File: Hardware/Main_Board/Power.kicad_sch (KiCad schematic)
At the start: 5 parts, among them U2 LM2596DSADJG

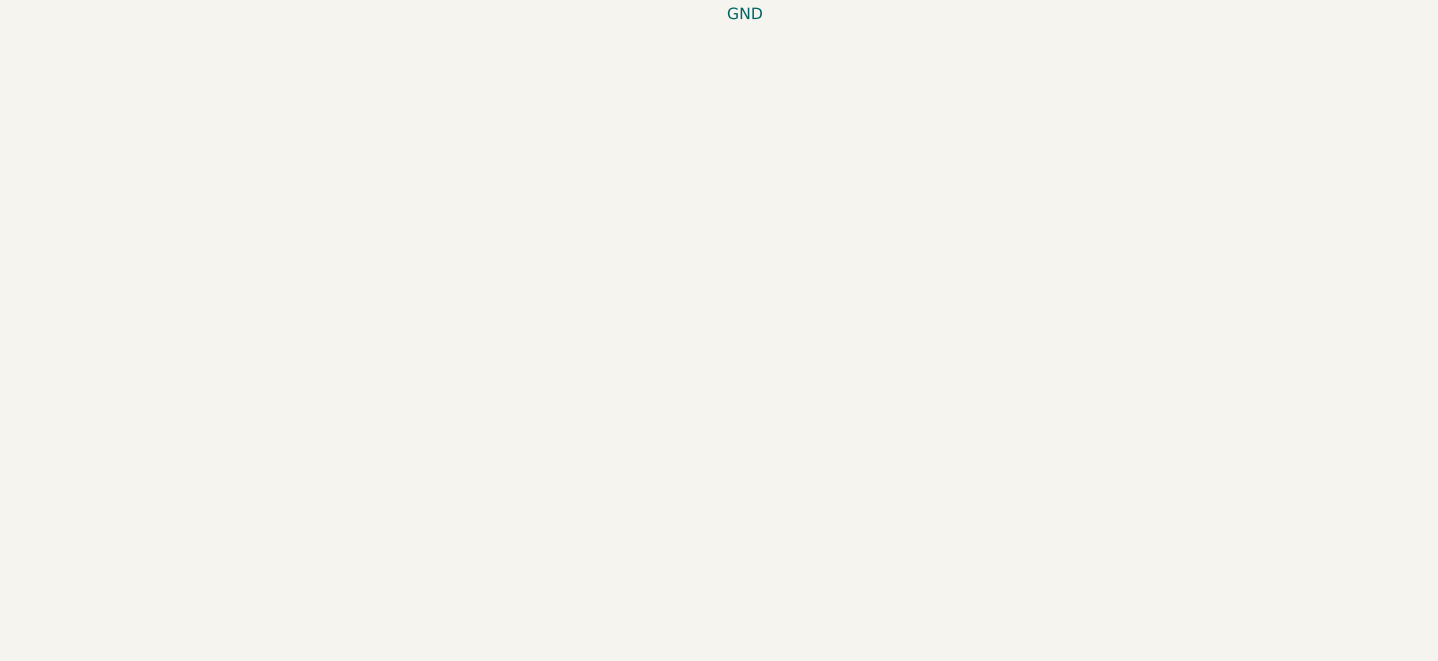
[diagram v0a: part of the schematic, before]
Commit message: Added the LDO on the Power schematic
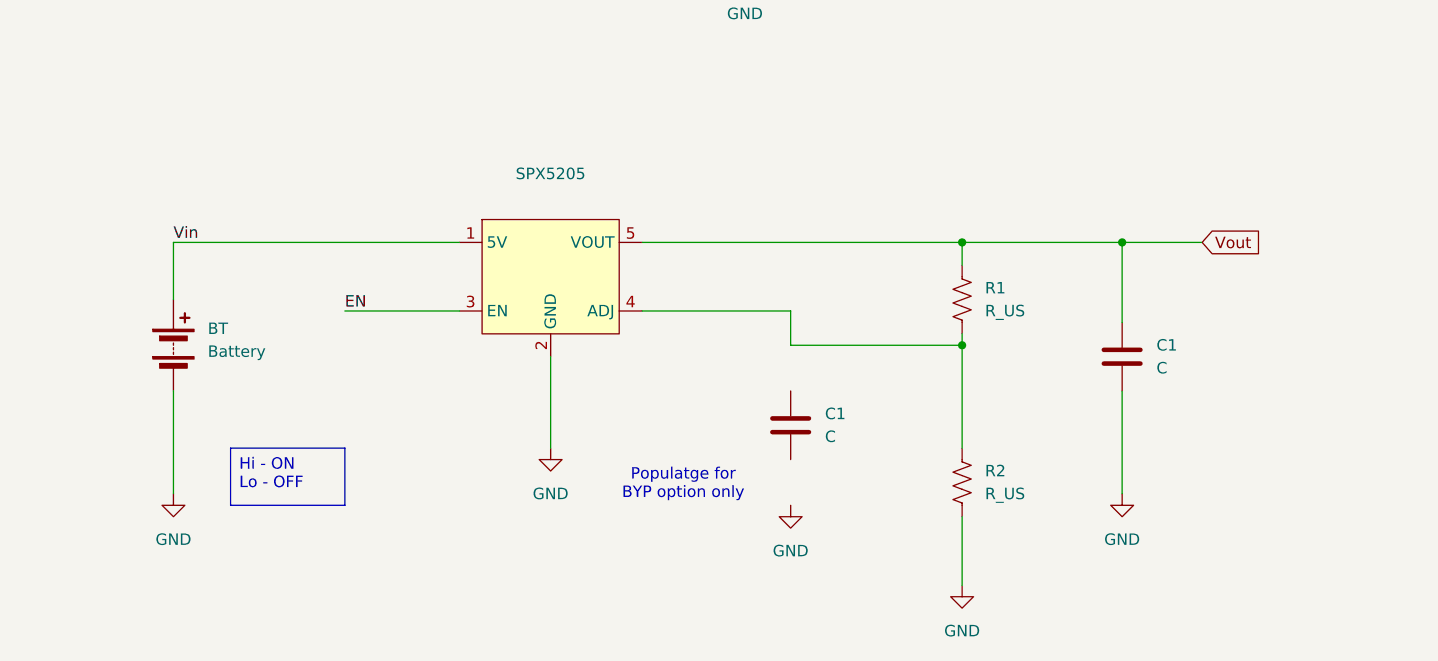
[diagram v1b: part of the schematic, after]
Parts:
- added BT: Battery, symbol Device:Battery
- added C1 (x2): C, symbol Device:C
- added R1, R2: R_US, symbol Device:R_US
- added SPX5205: ~, symbol ESP32-Symbols:SPX5205-ADJ
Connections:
- net GND: now also BT.2 (-), C1.2, R2.2, SPX5205.2 (GND)
- new net: R1.2, R2.1, SPX5205.4 (ADJ)
- new net EN: SPX5205.3 (EN)
- new net Vin: BT.1 (+), SPX5205.1 (5V)
- new net Vout: C1.1, R1.1, SPX5205.5 (VOUT)
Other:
- note added: "Populatge for BYP option only"
